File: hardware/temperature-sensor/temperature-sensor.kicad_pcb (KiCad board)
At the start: 2 copper layers, 56 x 56 mm, 69 parts, among them IC1 SHT40-CD1B-R3, IC2 MAX5969BETB+T, IC3 LV2862XLVDDCR, J1 1149611, J2 AMPHENOL_micro_usb_10118194-0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, T1 SM13126PEL, U1 STM32F407V_E-G_Tx, U2 LAN8720A, U3 FT230XS, Y1 CX2016FB25000C0FZZH1

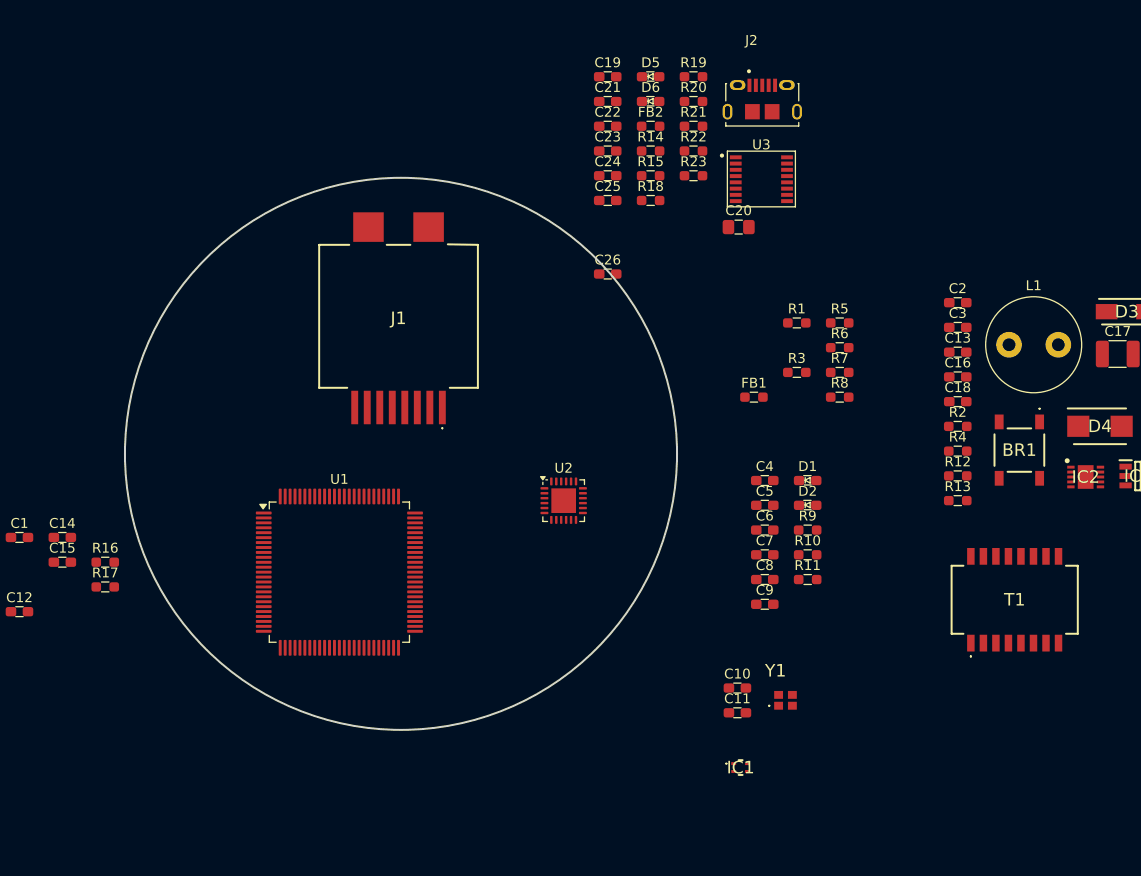
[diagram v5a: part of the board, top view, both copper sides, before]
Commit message: work on temperature sensor
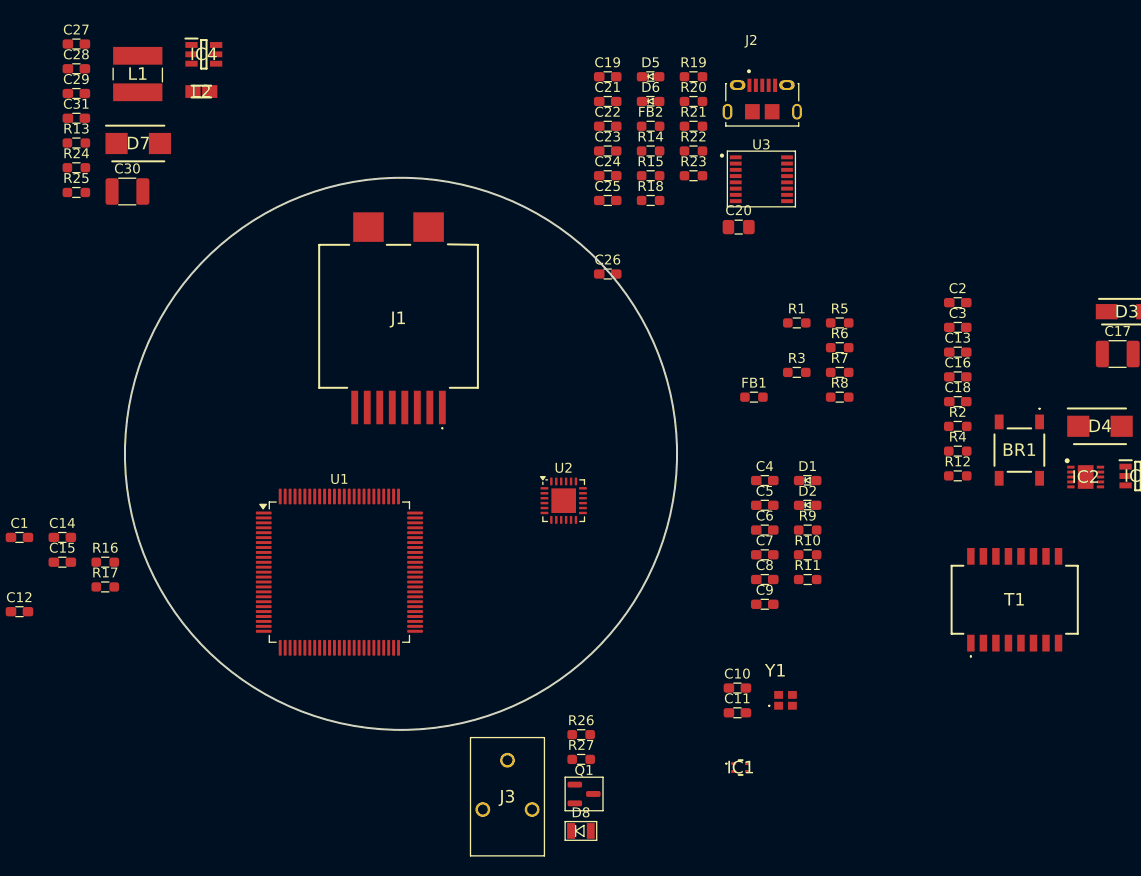
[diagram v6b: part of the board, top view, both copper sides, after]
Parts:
- added C27: 100nF, benediktibk:C_0603_1608Metric_Pad1.08x0.95mm_HandSolder, F.Cu at (117.1, 57.4)
- added C28: 1uF 100V, benediktibk:C_0603_1608Metric_Pad1.08x0.95mm_HandSolder, F.Cu at (117.1, 59.9)
- added C29: 1uF 100V, benediktibk:C_0603_1608Metric_Pad1.08x0.95mm_HandSolder, F.Cu at (117.1, 62.5)
- added C30: 10uF, benediktibk:C_1210_3225Metric_Pad1.33x2.70mm_HandSolder, F.Cu at (122.3, 72.4)
- added C31: 1uF, benediktibk:C_0603_1608Metric_Pad1.08x0.95mm_HandSolder, F.Cu at (117.1, 65.0)
- added D7: B280-13-F, benediktibk:DIOM5336X250N, F.Cu at (123.3, 67.5)
- added D8: BAT54WS, benediktibk:D_SOD-323, F.Cu at (168.2, 137.2)
- added IC4: LV2862XLVDDCR, benediktibk:SOT95P280X110-6N, F.Cu at (130.0, 58.5)
- added J3: 1990012, benediktibk:1990012, F.Cu at (160.8, 133.8)
- added L2: SRN2012T-6R8K, benediktibk:INDPM2012X120N, F.Cu at (129.8, 62.2)
- added Q1: DMN3404L, benediktibk:SOT-23, F.Cu at (168.6, 133.5)
- added R24: 33kOhm, benediktibk:R_0603_1608Metric_Pad0.98x0.95mm_HandSolder, F.Cu at (117.1, 70.0)
- added R25: 10kOhm, benediktibk:R_0603_1608Metric_Pad0.98x0.95mm_HandSolder, F.Cu at (117.1, 72.5)
- added R26: 10kOhm, benediktibk:R_0603_1608Metric_Pad0.98x0.95mm_HandSolder, F.Cu at (168.3, 127.5)
- added R27: 10kOhm, benediktibk:R_0603_1608Metric_Pad0.98x0.95mm_HandSolder, F.Cu at (168.3, 130.0)
- L1: value 22uH -> SDR0503-102KL; footprint benediktibk:L_Radial_D9.5mm_P5.00mm_Fastron_07HVP -> benediktibk:SDR0503102KL
- R13: value 33kOhm -> 147kOhm
- U2: footprint benediktibk:QFN-24-1EP_4x4mm_P0.5mm_EP2.5x2.5mm -> benediktibk:LAN8720A-CP-ABC
- moved R13 96.5 mm to (117.1, 67.5)
- moved L1 92.5 mm to (123.3, 60.5)
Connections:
- net /Ethernet/CLK renamed /Ethernet/25MHz
- net /Measurement/SCL renamed /MCU/SCL
- net /Measurement/SDA renamed /MCU/SDA
- net /Power over Ethernet/3V3 renamed /12V
- net /USB/UART_RX renamed /MCU/UART_TX
- net /USB/UART_TX renamed /MCU/UART_RX
- net Net-(BR1-+) renamed /Power over Ethernet/54V
- net Net-(IC2-PG) renamed /Power over Ethernet/PG
- BR1 pad 2: /Power over Ethernet/CT1 -> /Ethernet/CT1
- BR1 pad 3: /Power over Ethernet/CT2 -> /Ethernet/CT2
- BR1 pad 4: GND -> Net-(BR1--)
- C16 pad 2: GND -> Net-(BR1--)
- C26 pad 1: /Measurement/3V3 -> /3V3
- D3 pad 2: GND -> Net-(BR1--)
- FB1 pad 2: /Ethernet/3V3 -> /3V3
- IC1 pad 3: /Measurement/3V3 -> /3V3
- IC2 pad 11: GND -> Net-(BR1--)
- IC2 pad 5: unconnected-(IC2-VSS-Pad5) -> Net-(BR1--)
- IC2 pad 6: Net-(IC2-RTN) -> GND
- IC2 pad 7: Net-(IC2-RTN) -> GND
- R2 pad 2: GND -> Net-(BR1--)
- R20 pad 1: /USB/3V3 -> /3V3
- R21 pad 1: /USB/3V3 -> /3V3
- R22 pad 1: /USB/3V3 -> /3V3
- R23 pad 1: /USB/3V3 -> /3V3

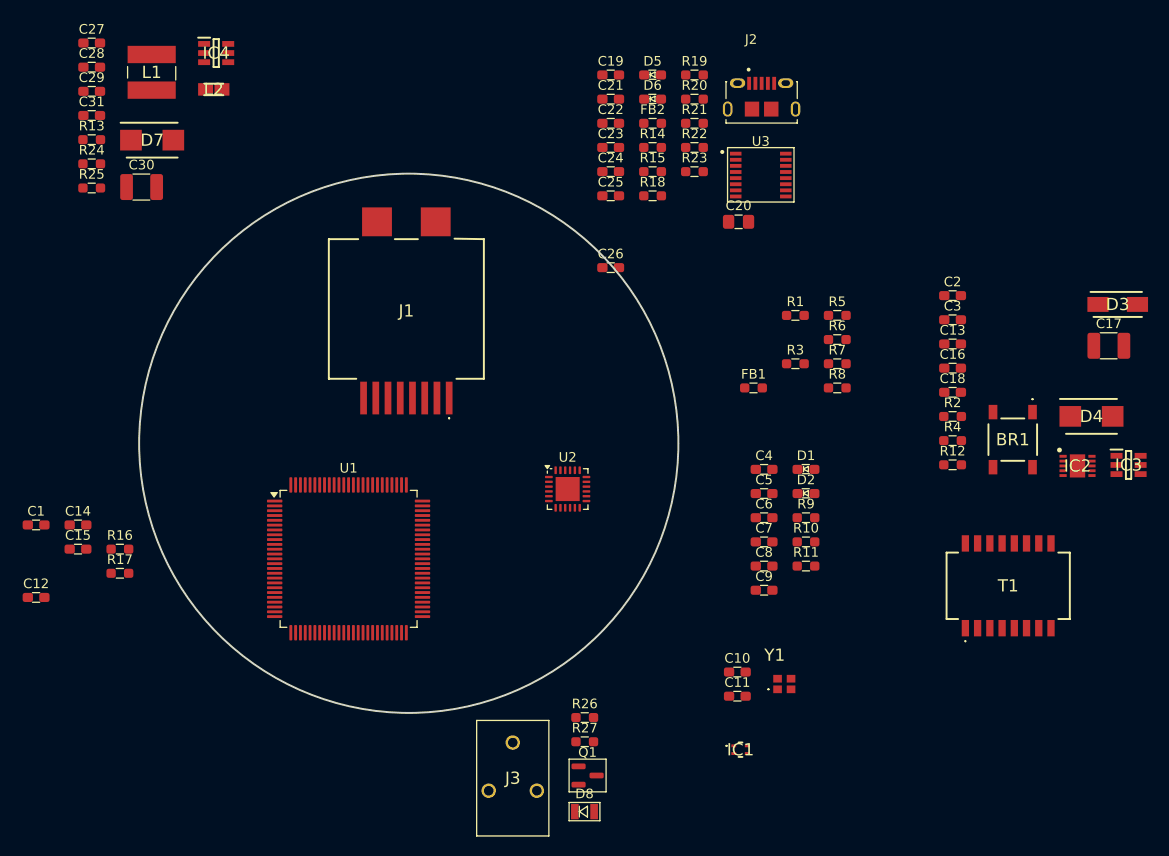
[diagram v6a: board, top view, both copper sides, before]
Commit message: replace USB micro with USB c
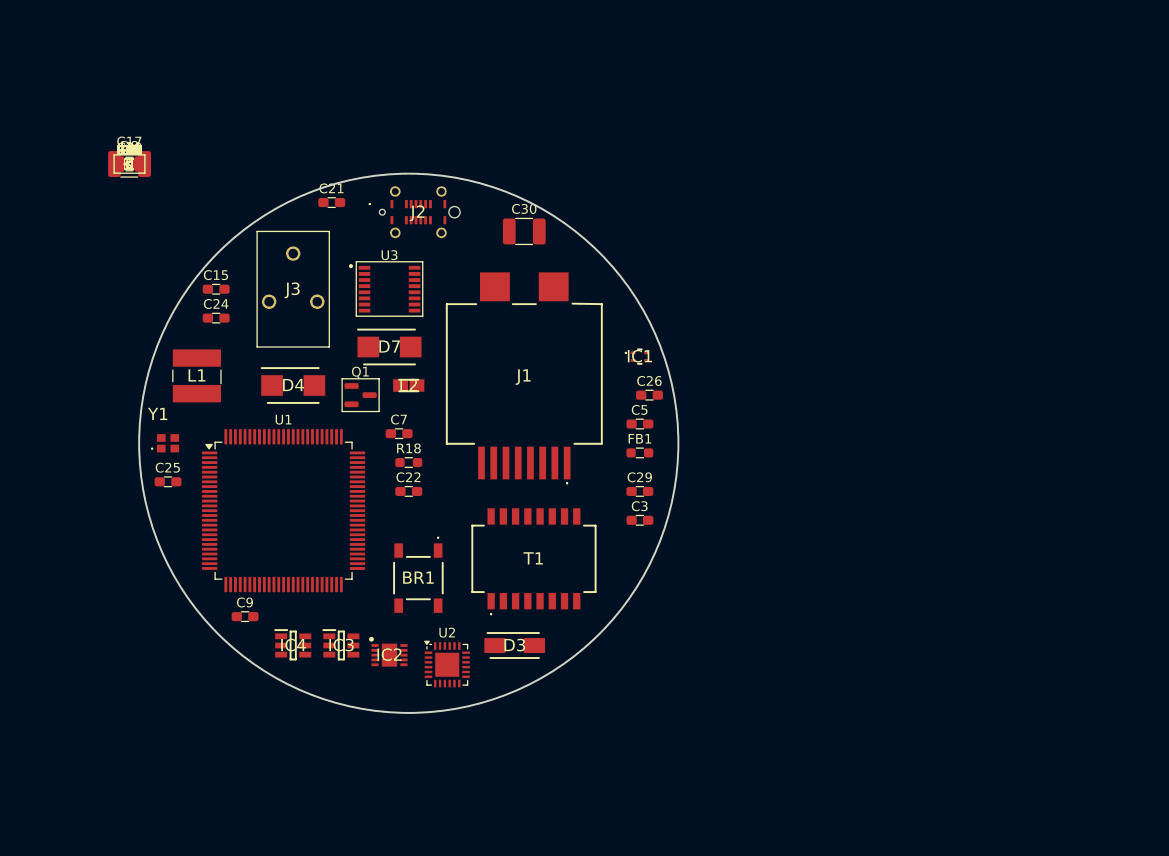
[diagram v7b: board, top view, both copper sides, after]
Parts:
- added C32: C_1nF_SMD_1812_3kV_10%, benediktibk:C_0603_1608Metric_Pad1.08x0.95mm_HandSolder, F.Cu at (121.0, 70.0)
- added R28, R29: 5.1kOhm, benediktibk:R_0603_1608Metric_Pad0.98x0.95mm_HandSolder, F.Cu at (121.0, 70.0)
- J2: value AMPHENOL_micro_usb_10118194-0001LF -> 219320-0001; footprint benediktibk:AMPHENOL_10118194-0001LF -> benediktibk:2193200001
- moved C17 103.4 mm to (121.0, 70.0)
- moved R12 91.0 mm to (121.0, 70.0)
- moved R4 90.2 mm to (121.0, 70.0)
- moved R2 89.4 mm to (121.0, 70.0)
- moved C18 88.7 mm to (121.0, 70.0)
- moved C16 88.1 mm to (121.0, 70.0)
- moved C13 87.5 mm to (121.0, 70.0)
- moved C2 86.6 mm to (121.0, 70.0)
- moved C11 83.9 mm to (121.0, 70.0)
- moved IC3 83.9 mm to (143.0, 120.0)
- moved D4 83.0 mm to (138.0, 93.0)
- moved C10 82.3 mm to (121.0, 70.0)
- moved D8 82.2 mm to (121.0, 70.0)
- moved R11 81.7 mm to (121.0, 70.0)
- moved R10 80.5 mm to (121.0, 70.0)
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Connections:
- C19 pad 1: Net-(J2-VCC) -> Net-(J2-VBUS_1)
- FB2 pad 1: Net-(J2-VCC) -> Net-(J2-VBUS_1)
- R14 pad 1: Net-(U3-USBDM) -> Net-(U3-USBDP)
- R14 pad 2: Net-(J2-D-) -> Net-(J2-DP1)
- R15 pad 1: Net-(U3-USBDP) -> Net-(U3-USBDM)
- R15 pad 2: Net-(J2-D+) -> Net-(J2-DN1)

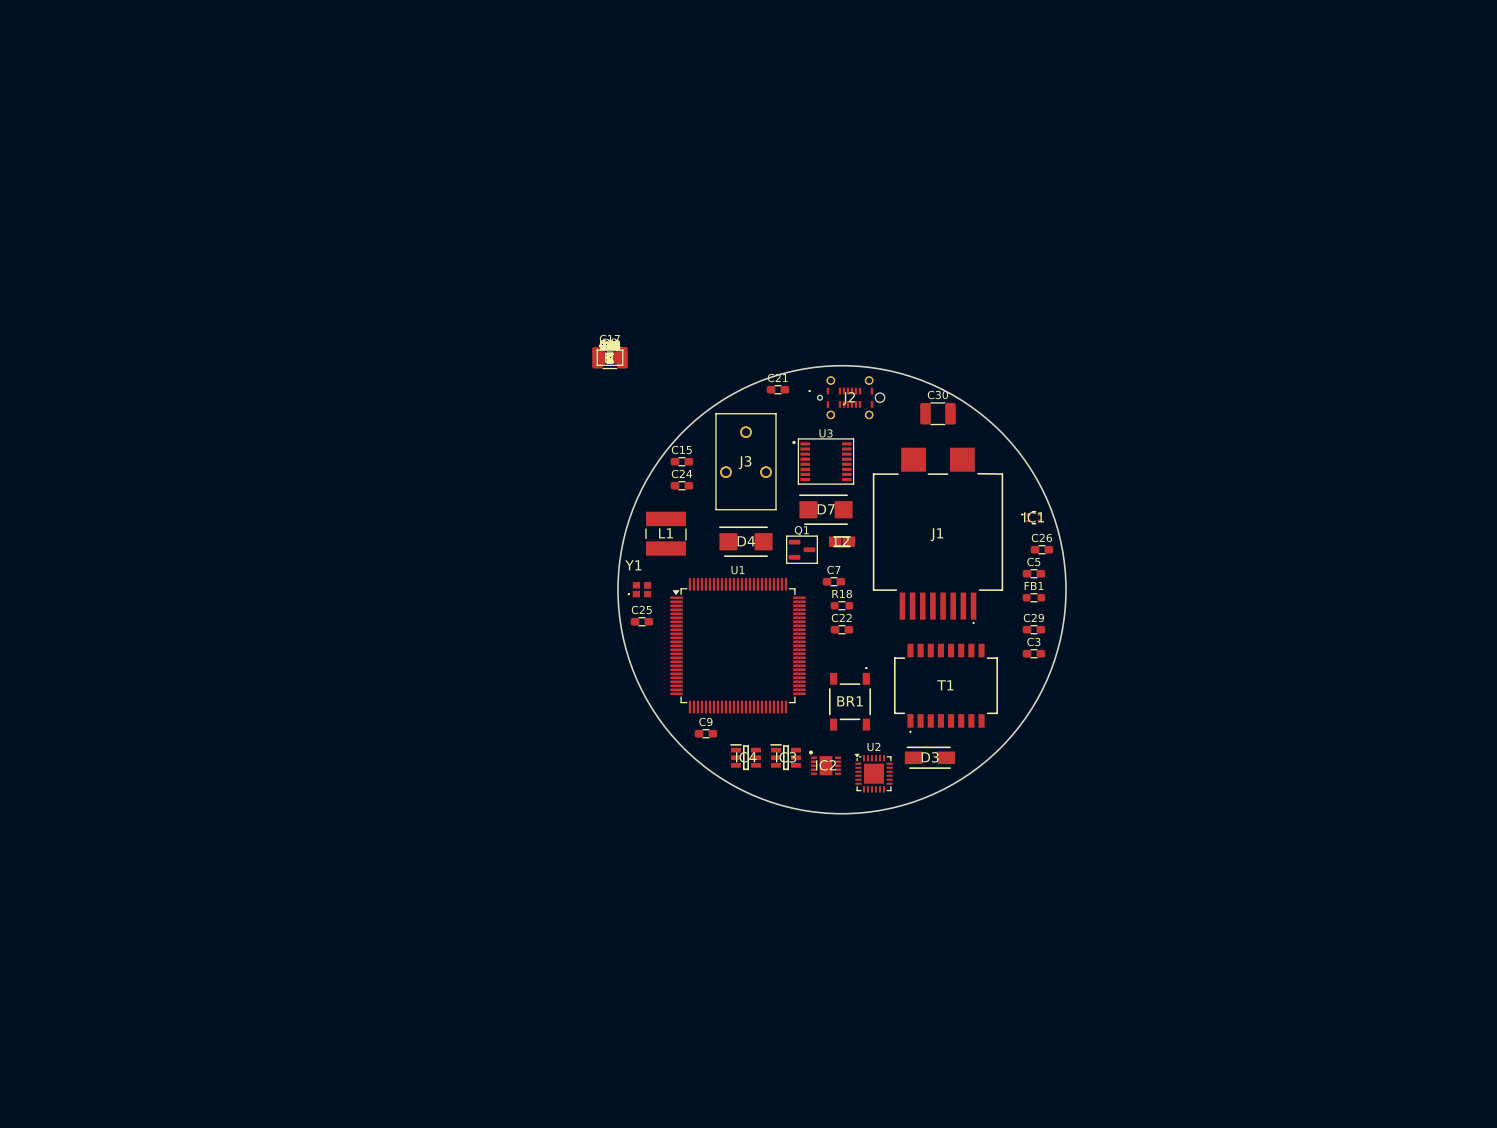
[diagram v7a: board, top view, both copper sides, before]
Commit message: start with layout of ethernet and PoE
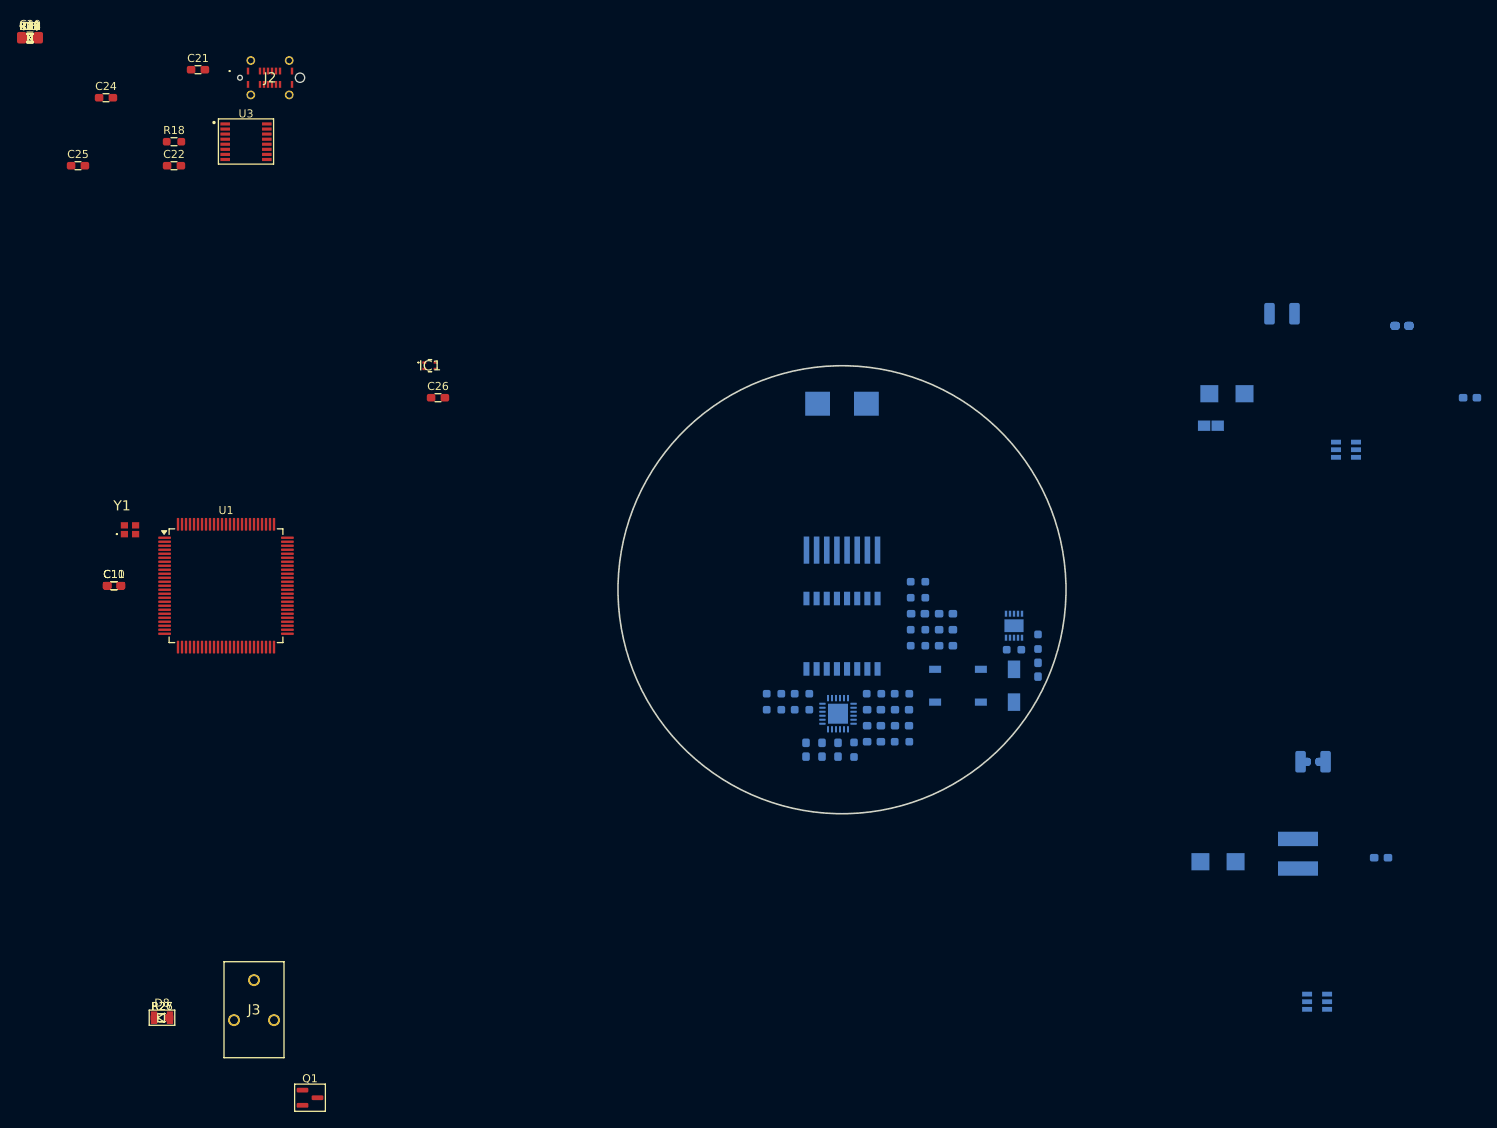
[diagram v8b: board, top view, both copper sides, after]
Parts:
- BR1, C1, C12, C13, C14, C15, C16, C17, C18, C2, C27, C28, C29, C3, C30, C31, C4, C5, C6, C7, C8, C9, D1, D2, D3, D4, D7, FB1, IC2, IC3, IC4, J1, L1, L2, R1, R10, R11, R12, R13, R16, R17, R2, R24, R25, R3, R4, R5, R6, R7, R8, R9, T1, U2: moved to B.Cu
- moved C22 101.7 mm to (66.5, 46.0)
- moved R18 101.7 mm to (66.5, 43.0)
- moved C13 101.4 mm to (208.9, 120.5), turned to 180 degrees
- moved C17 101.4 mm to (208.9, 120.5), turned to 180 degrees
- moved C18 101.4 mm to (208.9, 120.5), turned to 180 degrees
- moved C2 101.4 mm to (208.9, 120.5), turned to 180 degrees
- moved R12 101.4 mm to (208.9, 120.5), turned to 180 degrees
- moved R13 101.4 mm to (208.9, 120.5), turned to 180 degrees
- moved D8 99.7 mm to (65.0, 152.5)
- moved R26 99.7 mm to (65.0, 152.5)
- moved R27 99.7 mm to (65.0, 152.5)
- moved C27 99.1 mm to (220.0, 66.0), turned to 180 degrees
- moved C28 99.1 mm to (220.0, 66.0), turned to 180 degrees
- moved C31 99.1 mm to (220.0, 66.0), turned to 180 degrees
- moved R24 99.1 mm to (220.0, 66.0), turned to 180 degrees
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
